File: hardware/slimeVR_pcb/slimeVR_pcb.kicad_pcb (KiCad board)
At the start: 2 copper layers, 31 parts, among them J1 USB_C_Receptacle_USB2.0_16P, Q1 Q_Dual_NMOS_S1G1S2G2D2D2D1D1, SW1 SW_SPDT, SW2 SW_Push, SW3 SW_Push, U1 ESP32-S2-WROVER, U10 AP2112K-3.3, U2 TP4057, U3 BMI160, U4 ICM-20948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

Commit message: stuff
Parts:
- removed U6: MPU-6050, Sensor_Motion:InvenSense_QFN-24_4x4mm_P0.5mm
- removed U9: MMC5883MA, Package_LGA:LGA-16_3x3mm_P0.5mm
- added C2: 100n, Capacitor_SMD:C_0603_1608Metric_Pad1.08x0.95mm_HandSolder, F.Cu at (146.2, 65.9)
- added C3: 100n, Capacitor_SMD:C_0603_1608Metric_Pad1.08x0.95mm_HandSolder, F.Cu at (170.0, 48.1)
- added C4: 1u, Capacitor_SMD:C_0603_1608Metric_Pad1.08x0.95mm_HandSolder, F.Cu at (171.5, 48.1)
- added JP1: SolderJumper_2_Open, Jumper:SolderJumper-2_P1.3mm_Open_TrianglePad1.0x1.5mm, F.Cu at (176.3, 52.5)
- added R12: 1k, Resistor_SMD:R_0603_1608Metric_Pad0.98x0.95mm_HandSolder, F.Cu at (146.2, 59.9)
- added R13: 1k, Resistor_SMD:R_0603_1608Metric_Pad0.98x0.95mm_HandSolder, F.Cu at (146.2, 63.0)
- R8, R9: value 1k -> 5k1
- SW1: footprint Button_Switch_THT:SW_Slide_SPDT_Straight_CK_OS102011MS2Q -> Button_Switch_THT:SW_Slide_SPDT_Angled_CK_OS102011MA1Q
- U3: value BMI160 -> ICM-45686; footprint Package_LGA:Bosch_LGA-14_3x2.5mm_P0.5mm -> easyeda2kicad:LGA-14_L3.0-W2.5-P0.50-TL
- U4: value ICM-20948 -> LSM6DSRTR; footprint Sensor_Motion:InvenSense_QFN-24_3x3mm_P0.4mm -> easyeda2kicad:LGA-14_L3.0-W2.5-P0.50-BR
- U5: value MPU-9250 -> QMC6309; footprint Sensor_Motion:InvenSense_QFN-24_3x3mm_P0.4mm -> easyeda2kicad:X1-WLB0808-4_L0.8-W0.8-P0.40-TL
- moved C1 66.1 mm to (181.1, 68.0)
- moved D1 55.4 mm to (167.5, 75.5), turned to -90 degrees
- moved D3 54.8 mm to (146.0, 45.0)
- moved D2 52.9 mm to (164.5, 75.5), turned to -90 degrees
- moved R1 51.4 mm to (181.1, 66.0)
- moved R10 46.4 mm to (145.9, 47.0)
- moved R2 45.8 mm to (181.1, 70.0)
- moved R8 44.7 mm to (171.1, 57.9), turned to 180 degrees
- moved R9 39.5 mm to (171.1, 61.0), turned to 180 degrees
- moved SW3 33.6 mm to (154.9, 73.5), turned to 90 degrees
- moved R6 31.7 mm to (161.0, 75.5), turned to 90 degrees
- moved R7 30.7 mm to (161.0, 71.6), turned to -90 degrees
- moved R5 30.5 mm to (171.1, 64.0)
- moved R3 29.1 mm to (167.5, 71.6), turned to 90 degrees
- moved SW2 25.6 mm to (147.0, 73.5), turned to -90 degrees
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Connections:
- Q1 pad 6: Net-(Q1A-D-Pad8) -> Net-(Q1A-D-Pad7)
- Q1 pad 8: Net-(Q1A-D-Pad8) -> Net-(Q1A-D-Pad7)
- R2 pad 1: +BATT -> Net-(U7-VCC)
- R2 pad 2: Net-(U7-VCC) -> +BATT
- SW1 pad 1: +5V -> Net-(JP1-B)
- U3 pad 1: unconnected-(U3-SDO-Pad1) -> GND
- U3 pad 12: unconnected-(U3-CSB-Pad12) -> +3V3
- U3 pad 2: unconnected-(U3-ASDx-Pad2) -> /SDA_IMU
- U3 pad 3: unconnected-(U3-ASCx-Pad3) -> /SCL_IMU
- U3 pad 4: /INT_BMI_1 -> /INT
- U3 pad 6: unconnected-(U3-GNDIO-Pad6) -> GND
- U3 pad 9: /INT_BMI_2 -> unconnected-(U3-INT2/FSYNC/CLKIN-Pad9)
- U4 pad 1: unconnected-(U4-NC-Pad1) -> GND
- U4 pad 12: /INT_ICM -> +3V3
- U4 pad 13: +3V3 -> /SCL
- U4 pad 14: unconnected-(U4-NC-Pad14) -> /SDA
- U4 pad 2: unconnected-(U4-NC-Pad2) -> /SDA_IMU
- U4 pad 3: unconnected-(U4-NC-Pad3) -> /SCL_IMU
- U4 pad 4: unconnected-(U4-NC-Pad4) -> /INT
- U4 pad 5: unconnected-(U4-NC-Pad5) -> +3V3
- U4 pad 6: unconnected-(U4-NC-Pad6) -> GND
- U4 pad 7: unconnected-(U4-AUX_CL-Pad7) -> GND
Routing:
- net +BATT: track 0.00 -> 44.3 mm, vias 0 -> 1
- net +5V: track 0.00 -> 36.8 mm, vias 0 -> 2
- net /D-: track 0.00 -> 23.9 mm, vias 0 -> 2
- net /D+: track 0.00 -> 20.8 mm, vias 0 -> 2
- net -BATT: track 0.00 -> 17.6 mm
- net +3V3: track 0.00 -> 13.4 mm
- net /EN: track 0.00 -> 12.9 mm
- net /BAT_FULL: track 0.00 -> 9.79 mm
- net Net-(U7-CS): track 0.00 -> 9.35 mm
- net Net-(Q1A-G): track 0.00 -> 8.19 mm
- net Net-(Q1B-G): track 0.00 -> 5.91 mm
- net /BOOT: track 0.00 -> 5.08 mm
- net Net-(U7-VCC): track 0.00 -> 4.70 mm
- net GND: track 0.00 -> 4.65 mm, vias 0 -> 19
- net Net-(JP1-B): track 0.00 -> 4.57 mm
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- added copper zone on B.Cu, net GND
- added copper zone on F.Cu, net GND
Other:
- board outline added: 39 x 41 mm

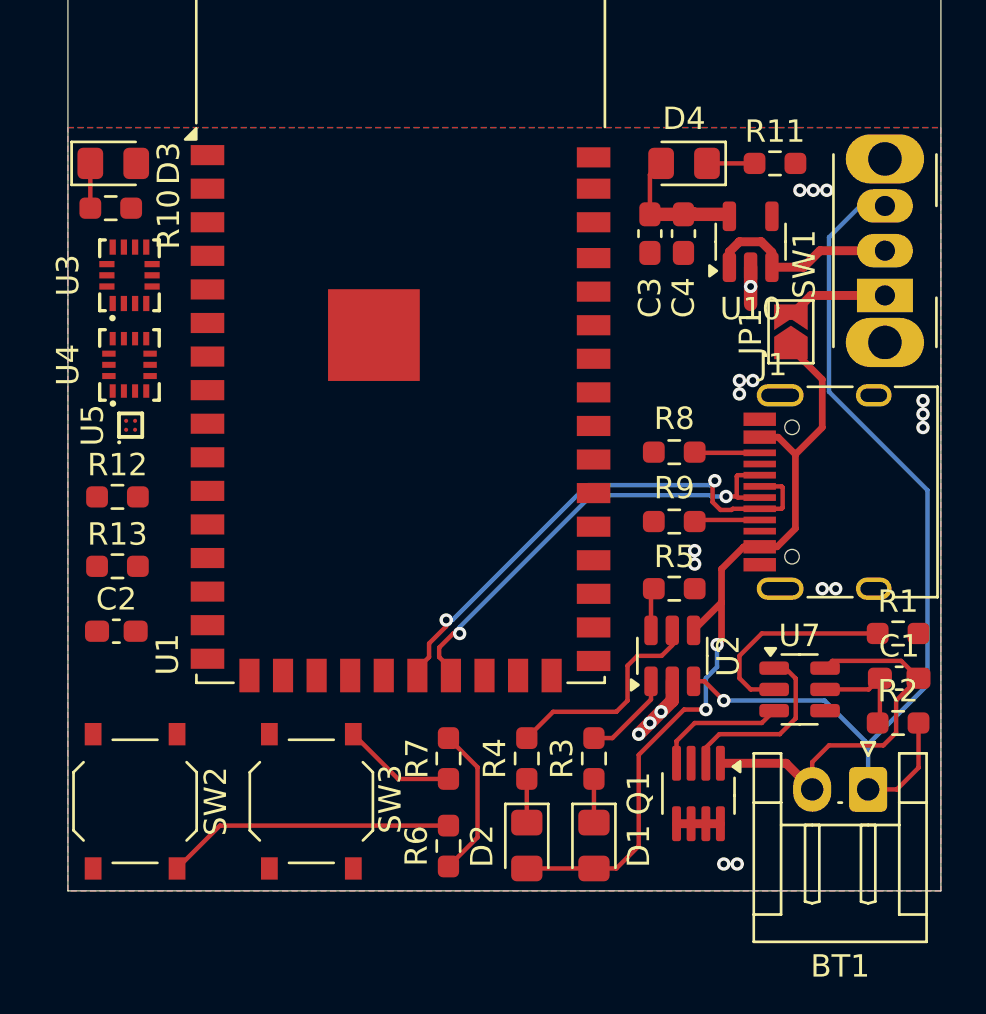
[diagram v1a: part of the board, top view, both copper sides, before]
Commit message: continue pcb, cleanup schematic
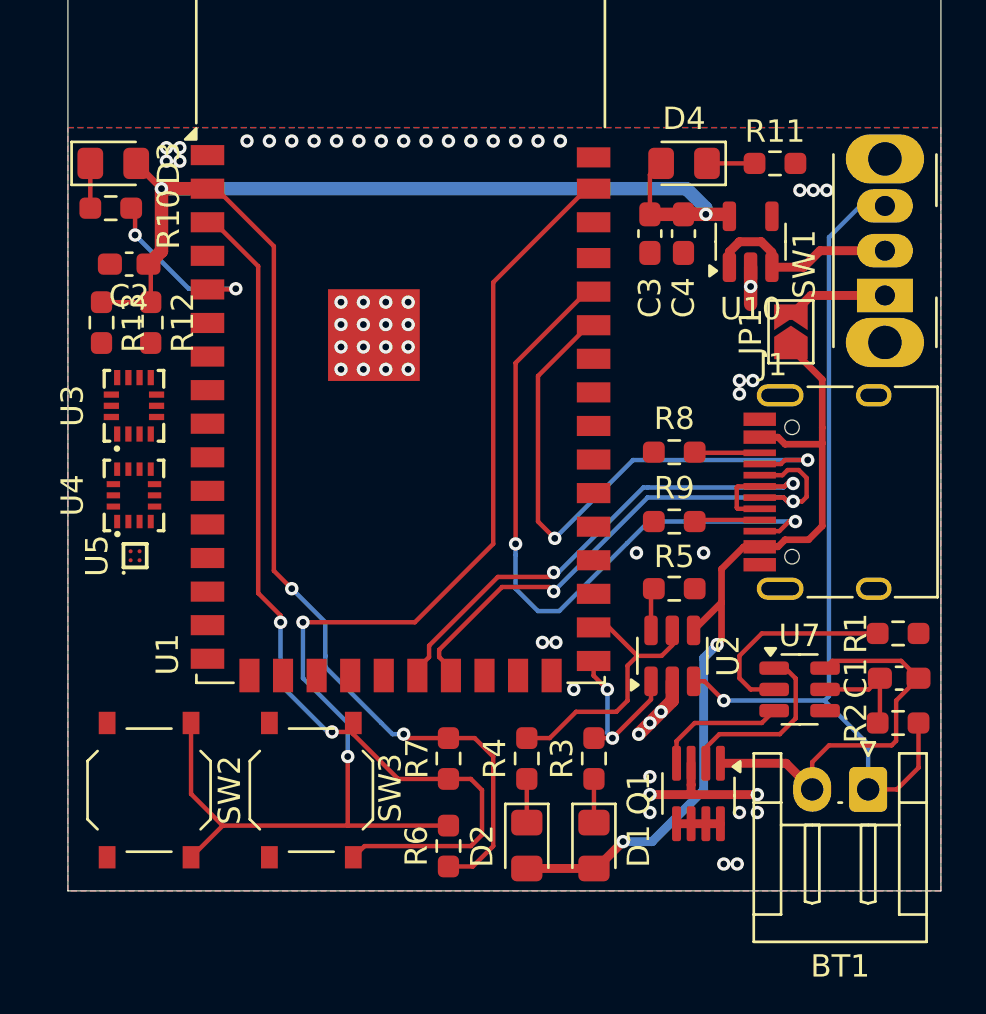
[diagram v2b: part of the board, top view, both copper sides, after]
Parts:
- moved C2 16.4 mm to (146.7, 49.5), turned to 180 degrees
- moved R13 10.9 mm to (145.5, 52.1), turned to -90 degrees
- moved R12 7.93 mm to (147.7, 52.1), turned to -90 degrees
- moved U3 5.83 mm to (146.9, 55.8)
- moved U4 5.83 mm to (146.9, 59.8)
- moved U5 5.83 mm to (147.0, 62.5)
- moved SW2 0.80 mm to (147.6, 73.0)
- moved SW3 0.50 mm to (154.9, 73.0)
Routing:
- net +3V3: track 13.4 -> 82.0 mm, vias 0 -> 4
- net /EN: track 12.9 -> 55.0 mm, vias 0 -> 2
- net /BOOT: track 5.08 -> 41.3 mm, vias 0 -> 2
- net /RX: track 0.00 -> 31.2 mm, vias 0 -> 2
- net /TX: track 0.00 -> 26.0 mm, vias 0 -> 2
- net Net-(U1-IO02): track 0.00 -> 8.04 mm, vias 0 -> 2
- net GND: track 4.65 -> 10.8 mm, vias 19 -> 58
- net /D+: track 20.8 -> 25.7 mm
- net +BATT: track 44.3 -> 39.5 mm
- net /BAT_CHG: track 4.08 -> 7.87 mm, vias 0 -> 2
- net /BAT_FULL: track 9.79 -> 12.3 mm
- net /D-: track 23.9 -> 25.4 mm
- net +5V: track 36.8 -> 38.1 mm

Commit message: add protection circuit
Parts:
- added JP2: SolderJumper_2_Open, Jumper:SolderJumper-2_P1.3mm_Open_TrianglePad1.0x1.5mm, B.Cu at (180.5, 59.8)
- added R14: 330k, Resistor_SMD:R_0603_1608Metric_Pad0.98x0.95mm_HandSolder, F.Cu at (171.1, 57.5)
- added R15: 150k, Resistor_SMD:R_0603_1608Metric_Pad0.98x0.95mm_HandSolder, F.Cu at (171.5, 52.5)
- added U6: TPS25200DRVR, Package_SON:WSON-6-1EP_2x2mm_P0.65mm_EP1x1.6mm_ThermalVias, F.Cu at (171.5, 55.1)
- moved R8 1.60 mm to (171.1, 59.5)
- moved D1 0.25 mm to (167.5, 75.2)
- moved D2 0.25 mm to (164.5, 75.2)
- moved R6 0.11 mm to (161.0, 75.4)
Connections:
- J1 pad A4: +5V -> VBUS
- J1 pad A9: +5V -> VBUS
- J1 pad B4: +5V -> VBUS
- J1 pad B9: +5V -> VBUS
- U1 pad 9: unconnected-(U1-IO06-Pad9) -> /INT
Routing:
- net VBUS: track 0.00 -> 17.3 mm, vias 0 -> 1
- net +5V: track 38.1 -> 42.5 mm, vias 2 -> 3
- net Net-(U6-ILIM): track 0.00 -> 2.10 mm
- net Net-(U6-EN): track 0.00 -> 1.78 mm
- net Net-(J1-CC2): track 2.92 -> 3.56 mm
- net GND: vias 58 -> 57

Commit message: cleanup pcb
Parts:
- removed R6: 1k, Resistor_SMD:R_0603_1608Metric_Pad0.98x0.95mm_HandSolder
- removed SW2: SW_Push, Button_Switch_SMD:SW_Push_1P1T_XKB_TS-1187A
- added TP1: GND, TestPoint:TestPoint_Pad_4.0x4.0mm, B.Cu at (147.2, 74.5)
- added TP2: +5V, TestPoint:TestPoint_Pad_4.0x4.0mm, B.Cu at (153.2, 74.5)
- D1: value LED -> red
- D2: value LED -> blue
- D3: value LED -> green
- D4: value LED -> white
- SW3: footprint Button_Switch_SMD:SW_Push_1P1T_XKB_TS-1187A -> Button_Switch_SMD:SW_Push_1P1T_NO_CK_KSC7xxJ
- moved R7 24.7 mm to (146.6, 51.5), turned to 0 degrees
- moved U3 6.17 mm to (146.9, 62.0)
- moved U4 6.17 mm to (146.9, 66.0)
- moved U5 6.17 mm to (147.0, 68.7)
- moved R12 3.46 mm to (145.5, 54.8)
- moved R13 3.34 mm to (147.5, 54.8)
- moved SW3 2.18 mm to (157.0, 73.5), turned to 180 degrees
- moved C2 0.24 mm to (146.5, 49.5)
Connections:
- U1 pad 41: /EN -> +3V3
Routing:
- net /EN: track 55.0 -> 0.00 mm, vias 2 -> 0
- net +3V3: track 82.0 -> 53.6 mm
- net +5V: track 42.5 -> 59.4 mm
- net /SDA: track 0.00 -> 5.59 mm
- net /BOOT: track 41.3 -> 37.3 mm
- net /SCL: track 0.00 -> 2.97 mm
- net GND: vias 57 -> 58

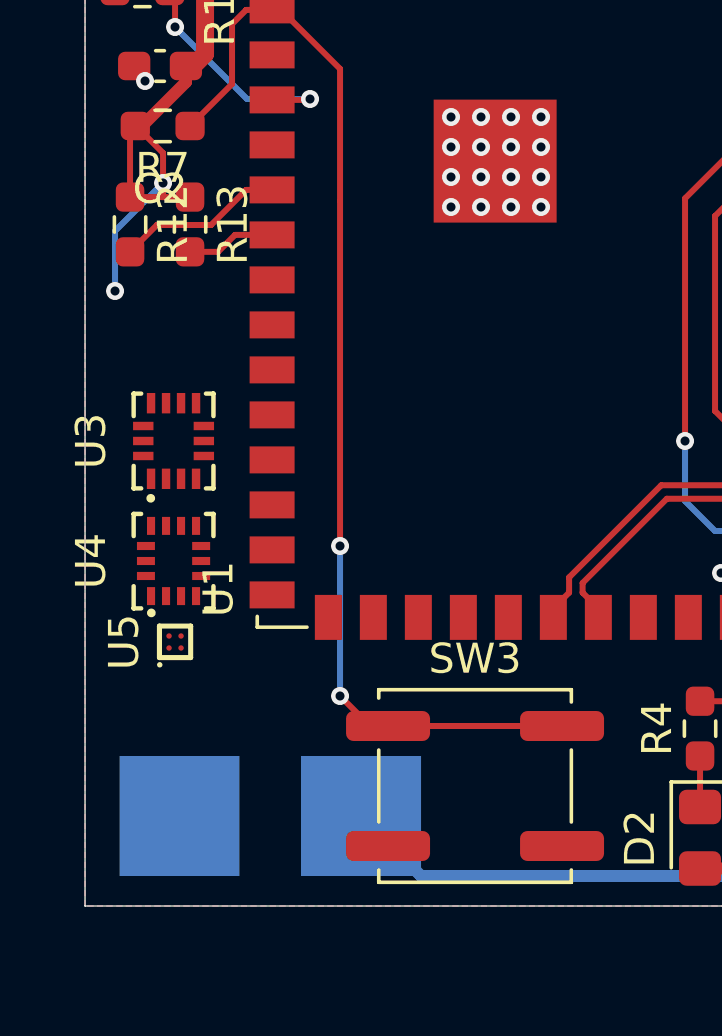
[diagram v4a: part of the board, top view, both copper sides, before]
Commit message: routed IMU
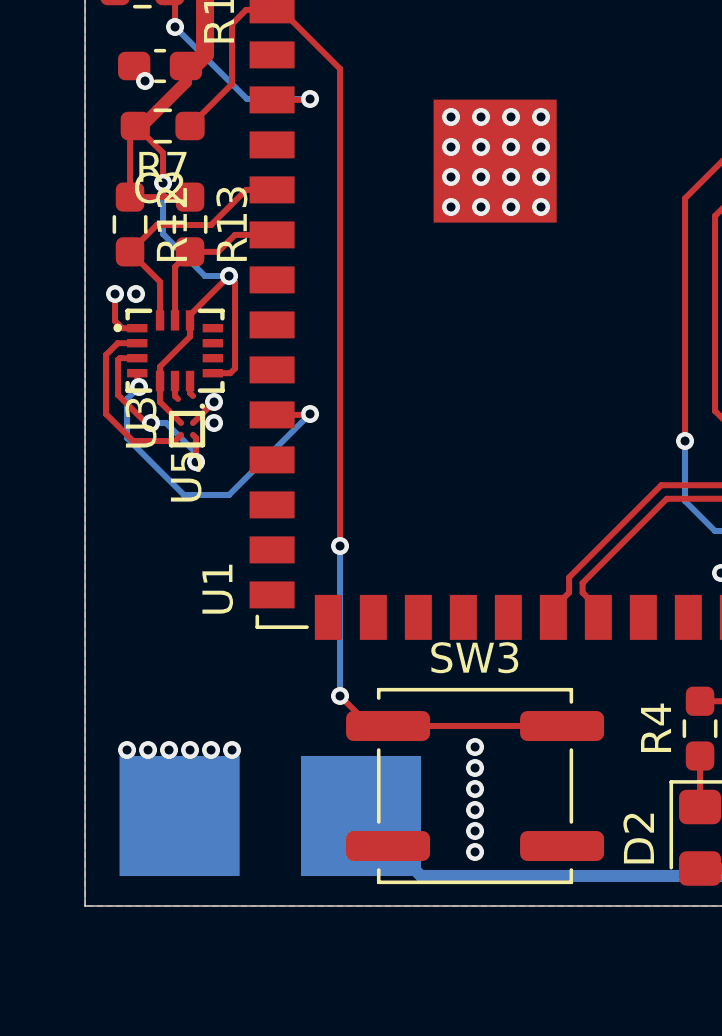
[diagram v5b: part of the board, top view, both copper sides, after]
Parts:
- removed U4: LSM6DSRTR, easyeda2kicad:LGA-14_L3.0-W2.5-P0.50-BR
- moved U5 7.11 mm to (147.4, 61.6), turned to -90 degrees
- moved U3 3.01 mm to (147.0, 59.0), turned to 0 degrees
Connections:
- U1 pad 12: unconnected-(U1-IO09-Pad12) -> /INT
- U1 pad 9: /INT -> unconnected-(U1-IO06-Pad9)
- U3 pad 7: unconnected-(U3-RESV-Pad7) -> GND
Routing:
- net /INT: track 0.00 -> 11.6 mm, vias 0 -> 2
- net +3V3: track 53.6 -> 64.0 mm
- net /SCL_IMU: track 0.00 -> 6.48 mm, vias 0 -> 2
- net /SDA_IMU: track 0.00 -> 6.13 mm
- net GND: track 10.8 -> 14.8 mm, vias 58 -> 74
- net /SDA: track 5.59 -> 8.29 mm
- net /SCL: track 2.97 -> 5.46 mm

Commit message: fix DRC, cleanup
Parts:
- U6: footprint Package_SON:WSON-6-1EP_2x2mm_P0.65mm_EP1x1.6mm_ThermalVias -> Package_SON:WSON-6-1EP_2x2mm_P0.65mm_EP1x1.6mm
- moved SW1 0.50 mm to (180.5, 50.4)
- moved C1 0.20 mm to (180.9, 68.0)
- moved D3 0.15 mm to (146.2, 45.0)
- moved R1 0.10 mm to (181.0, 66.0)
- moved R2 0.10 mm to (181.0, 70.0)
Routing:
- net GND: track 14.8 -> 15.6 mm, vias 74 -> 75

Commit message: tiredly add testpads
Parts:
- added TP3: SDA, TestPoint:TestPoint_Pad_D1.0mm, B.Cu at (151.5, 53.5)
- added TP4: SCL, TestPoint:TestPoint_Pad_D1.0mm, B.Cu at (151.5, 55.5)
- added TP5: INT, TestPoint:TestPoint_Pad_D1.0mm, B.Cu at (151.5, 61.1)
- added TP6: iSDA, TestPoint:TestPoint_Pad_D1.0mm, B.Cu at (145.5, 64.2)
- added TP7: iSCL, TestPoint:TestPoint_Pad_D1.0mm, B.Cu at (147.7, 62.7)
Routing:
- net /SDA_IMU: track 6.13 -> 8.58 mm, vias 0 -> 1
- net /SCL: track 5.46 -> 6.88 mm, vias 0 -> 1
- net /SDA: track 8.29 -> 9.61 mm, vias 0 -> 1
- net /INT: track 11.6 -> 12.2 mm

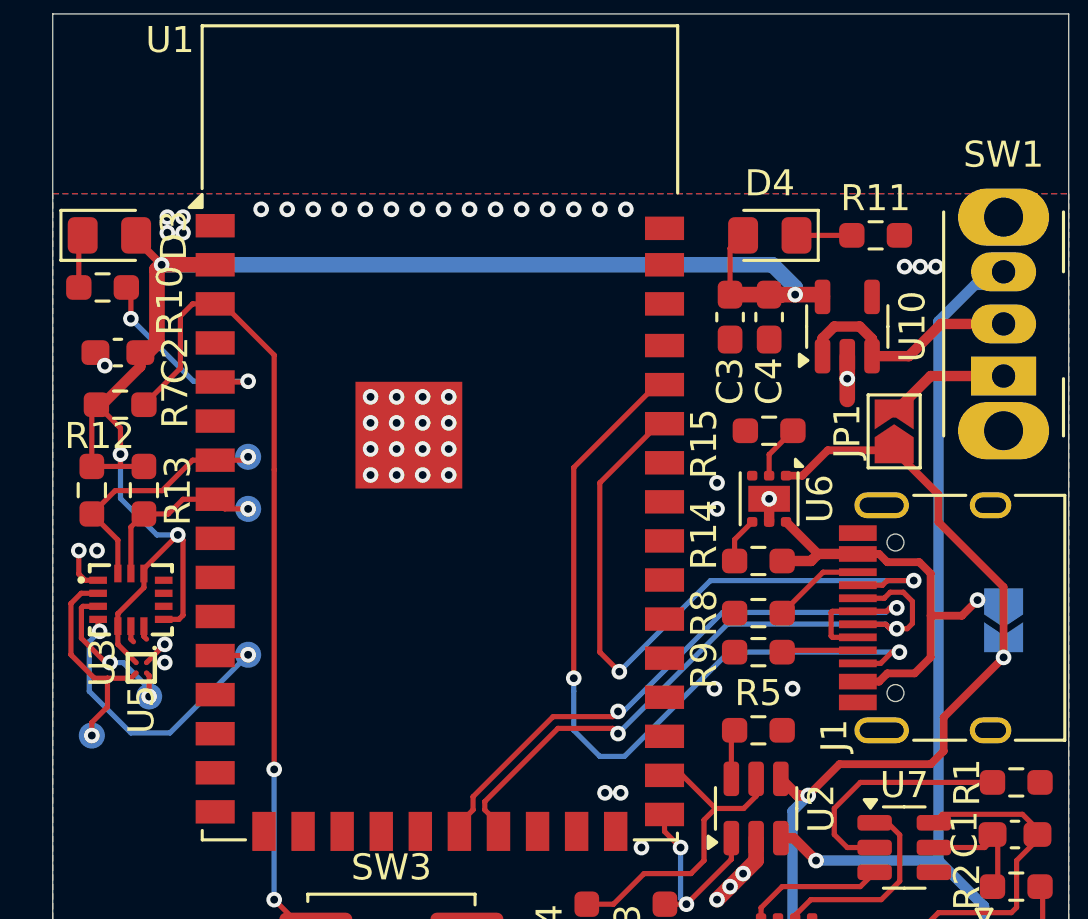
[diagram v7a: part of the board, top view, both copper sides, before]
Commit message: more testpad
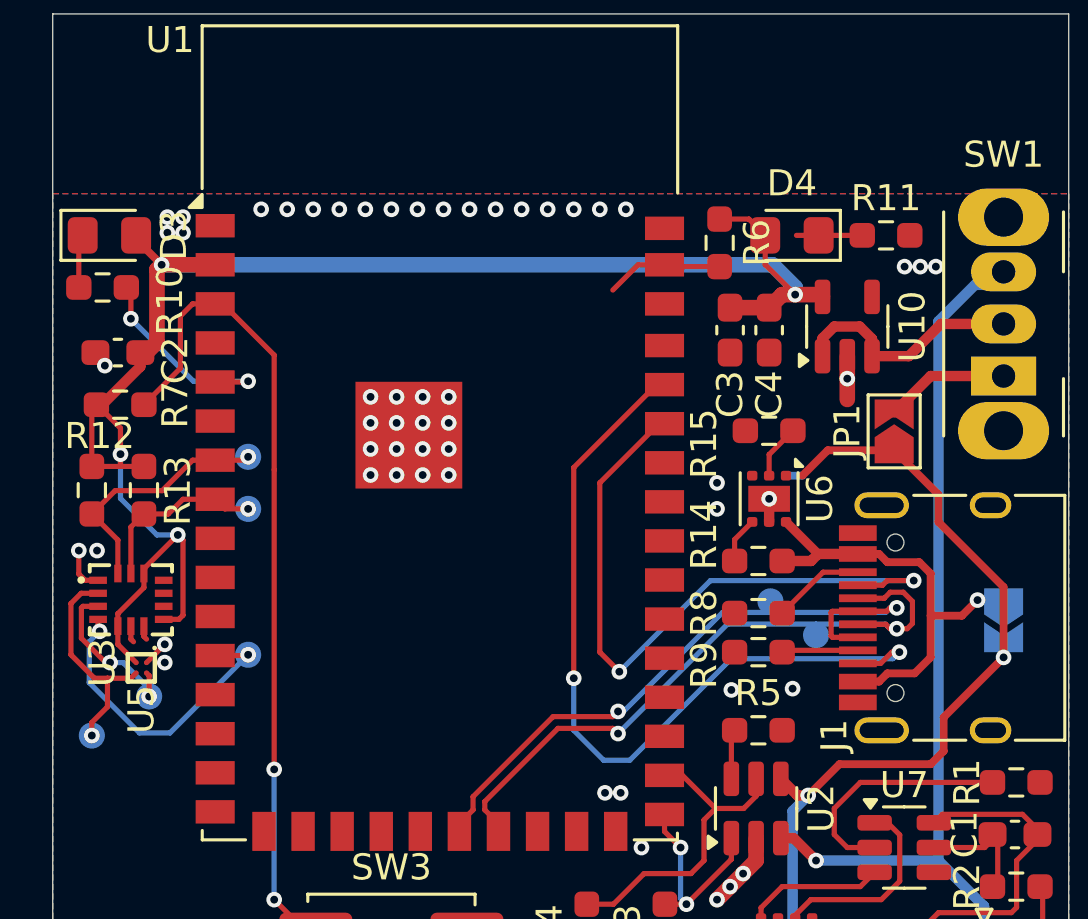
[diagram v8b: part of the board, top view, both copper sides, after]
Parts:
- added R6: 1k, Resistor_SMD:R_0603_1608Metric_Pad0.98x0.95mm_HandSolder, F.Cu at (169.6, 45.3)
- added TP8: D-, TestPoint:TestPoint_Pad_D1.0mm, B.Cu at (171.6, 59.0)
- added TP9: D+, TestPoint:TestPoint_Pad_D1.0mm, B.Cu at (173.3, 60.4)
- moved D4 0.85 mm to (172.4, 45.0)
- moved C3 0.50 mm to (170.0, 48.6)
- moved C4 0.50 mm to (171.5, 48.6)
- moved R11 0.40 mm to (176.0, 45.0)
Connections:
- U1 pad 33: unconnected-(U1-IO39-Pad33) -> /TCK
- U1 pad 34: unconnected-(U1-IO40-Pad34) -> /TDO
- U1 pad 35: unconnected-(U1-IO41-Pad35) -> /TDI
- U1 pad 36: unconnected-(U1-IO42-Pad36) -> /TMS
- U1 pad 41: +3V3 -> /EN
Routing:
- net /EN: track 0.00 -> 4.53 mm
- net +3V3: track 64.0 -> 65.9 mm
